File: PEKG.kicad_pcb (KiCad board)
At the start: 2 copper layers, 90 x 45 mm, 116 parts, among them J1 AudioJack4, J2 AudioJack3_SwitchTR, U1 TLV9062, U12 NCS21802DMR2G, U13 NCS21802DMR2G, U2 TLV9062, U3 INA350CDSIDDFR, U7 TLV61070ADBVR, U8 NCS21802DMR2G

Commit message: added sw
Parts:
- removed C21: 10n, Capacitor_SMD:C_0603_1608Metric_Pad1.08x0.95mm_HandSolder
- removed C22, C41: 10u, Capacitor_SMD:C_0603_1608Metric_Pad1.08x0.95mm_HandSolder
- removed C46: 100n, Capacitor_SMD:C_0603_1608Metric_Pad1.08x0.95mm_HandSolder
- removed JP1, JP7: Jumper_2_Bridged, Jumper:SolderJumper-2_P1.3mm_Bridged_RoundedPad1.0x1.5mm
- removed JP10, JP2, JP8: Jumper_2_Open, Jumper:SolderJumper-2_P1.3mm_Open_RoundedPad1.0x1.5mm
- removed L3: 4.7u, Inductor_SMD:L_Bourns_SRN6045TA
- removed R23, R32, R57: 100k, Resistor_SMD:R_0603_1608Metric_Pad0.98x0.95mm_HandSolder
- removed R35, R62, R63: 10k, Resistor_SMD:R_0603_1608Metric_Pad0.98x0.95mm_HandSolder
- removed R61: 1Meg, Resistor_SMD:R_0603_1608Metric_Pad0.98x0.95mm_HandSolder
- removed TP11: TestPoint, TestPoint:TestPoint_Pad_D3.0mm
- removed U13: NCS21802DMR2G, Package_SO:OnSemi_Micro8
- removed U3: INA350CDSIDDFR, Package_SO:MSOP-8_3x3mm_P0.65mm
- removed U7: TLV61070ADBVR, Package_TO_SOT_SMD:SOT-23-6_Handsoldering
- added SW1: SW_DPDT_x2, PEKG:DPDT_bigger, F.Cu at (159.0, 150.9)
- added U4: TLV9062, Package_SO:SOIC-8_3.9x4.9mm_P1.27mm, F.Cu at (152.3, 86.6)
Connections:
- net GAIN_5000_OUTPUT renamed GAIN_50
- C16 pad 2: Net-(U1A--) -> Net-(U12B--)
- C28 pad 2: Net-(JP2-A) -> DC_COMPENSATION
- JP3 pad 1: GAIN_500_OUTPUT -> GAIN_5
- JP9 pad 2: GAIN_500_OUTPUT -> GAIN_5
- R26 pad 2: Net-(U1A--) -> Net-(U12B--)
- R51 pad 1: Net-(U1A--) -> Net-(U12B--)
- R55 pad 2: Net-(JP2-A) -> DC_COMPENSATION
- R60 pad 1: Net-(U1A--) -> Net-(U12B--)
- U1 pad 1: Net-(JP4-A) -> (no net)
- U1 pad 2: Net-(U1A--) -> (no net)
- U1 pad 3: GAIN_500_OUTPUT -> (no net)
- U1 pad 5: GAIN_50_OUTPUT -> (no net)
- U1 pad 6: Net-(U1B--) -> (no net)
- U1 pad 7: Net-(JP10-A) -> (no net)
- U12 pad 5: V_{ref} -> GAIN_5
- U12 pad 6: COMMON_INPUT_LEVEL -> Net-(U12B--)
- U12 pad 7: Net-(C25-Pad2) -> Net-(JP4-A)
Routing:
- net (no net): track 0.00 -> 52.4 mm, vias 0 -> 2
- net GAIN_50_OUTPUT: track 29.6 -> 0.00 mm, vias 2 -> 0
- net GAIN_500_OUTPUT: track 13.5 -> 0.00 mm
- net GAIN_5: track 0.00 -> 13.5 mm
- net Net-(JP2-A): track 10.2 -> 0.00 mm
- net DC_COMPENSATION: track 42.4 -> 52.6 mm
- net Net-(JP10-A): track 9.98 -> 0.00 mm
- net Net-(U1B--): track 6.79 -> 0.00 mm
- net Net-(U1A--): track 6.75 -> 0.00 mm
- net Net-(U12B--): track 0.00 -> 6.75 mm
- net /FB: track 3.86 -> 0.00 mm
- net /SW_OUT: track 2.11 -> 0.00 mm
- added copper zone on F.Cu, net (none)
- removed copper zone on F.Cu, net /SW
- removed copper zone on F.Cu, net /SW_OUT

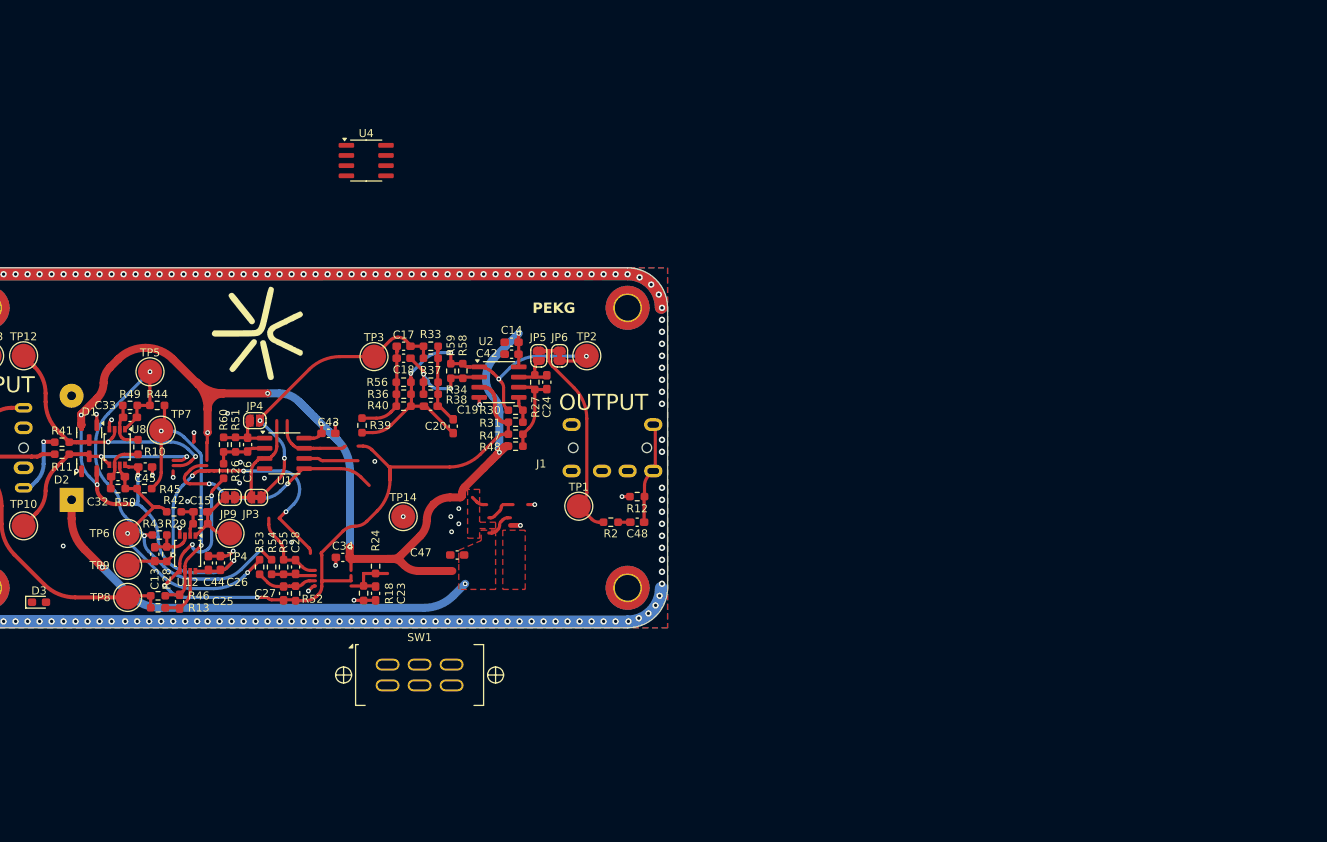
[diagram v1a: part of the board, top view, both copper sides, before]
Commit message: added notes, changed opamps
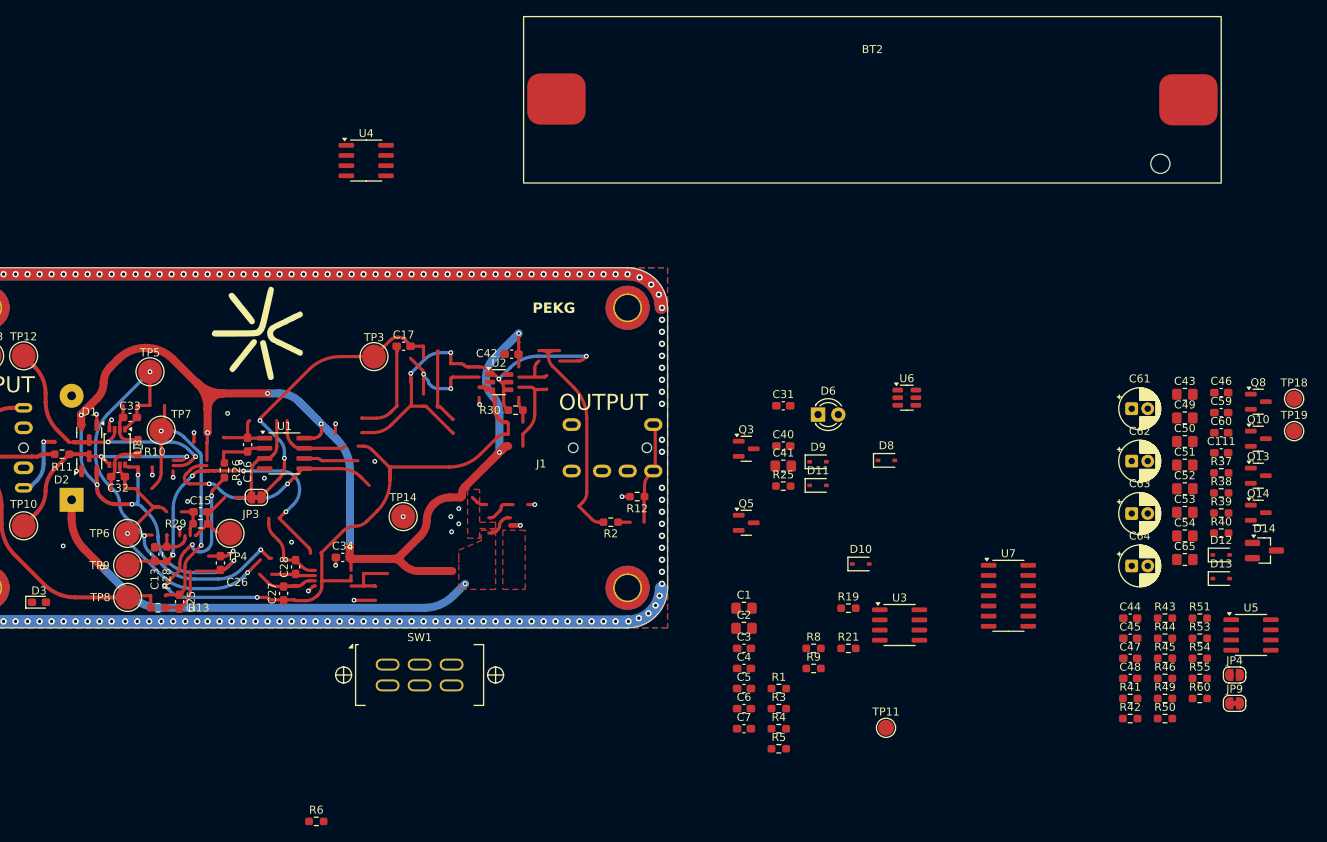
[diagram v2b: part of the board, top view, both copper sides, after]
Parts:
- removed C14, C23: 10u, Capacitor_SMD:C_0603_1608Metric_Pad1.08x0.95mm_HandSolder
- removed C18, C19, C20, C24: 10n, Capacitor_SMD:C_0603_1608Metric_Pad1.08x0.95mm_HandSolder
- removed JP5: Jumper_2_Open, Jumper:SolderJumper-2_P1.3mm_Open_RoundedPad1.0x1.5mm
- removed JP6: Jumper_2_Bridged, Jumper:SolderJumper-2_P1.3mm_Bridged_RoundedPad1.0x1.5mm
- removed R18, R24, R52: 100k, Resistor_SMD:R_0603_1608Metric_Pad0.98x0.95mm_HandSolder
- removed R27, R31: 10k, Resistor_SMD:R_0603_1608Metric_Pad0.98x0.95mm_HandSolder
- removed R33, R34, R56, R59: 10Meg, Resistor_SMD:R_0603_1608Metric_Pad0.98x0.95mm_HandSolder
- removed R36, R58: 330k, Resistor_SMD:R_0603_1608Metric_Pad0.98x0.95mm_HandSolder
- removed R47, R48: 20k, Resistor_SMD:R_0603_1608Metric_Pad0.98x0.95mm_HandSolder
- removed TP1, TP2: TestPoint, TestPoint:TestPoint_Pad_D3.0mm
- removed U12: NCS21802DMR2G, Package_SO:OnSemi_Micro8
- added BT2: Battery_Cell, PEKG:battery_holder, F.Cu at (215.6, 79.0)
- added C1: 10u, Resistor_SMD:R_0805_2012Metric_Pad1.20x1.40mm_HandSolder, F.Cu at (199.6, 142.6)
- added C111: 100n, Capacitor_SMD:C_0603_1608Metric_Pad1.08x0.95mm_HandSolder, F.Cu at (259.2, 123.1)
- added C2: 10u, Resistor_SMD:R_0805_2012Metric_Pad1.20x1.40mm_HandSolder, F.Cu at (199.6, 145.1)
- added C3: 100n, Capacitor_SMD:C_0603_1608Metric_Pad1.08x0.95mm_HandSolder, F.Cu at (199.6, 147.6)
- added C31: 100n, Capacitor_SMD:C_0603_1608Metric_Pad1.08x0.95mm_HandSolder, F.Cu at (204.5, 117.2)
- added C4: 100n, Capacitor_SMD:C_0603_1608Metric_Pad1.08x0.95mm_HandSolder, F.Cu at (199.6, 150.1)
- added C40: 1u, Capacitor_SMD:C_0603_1608Metric_Pad1.08x0.95mm_HandSolder, F.Cu at (204.5, 122.3)
- added C41: 10u, Resistor_SMD:R_0805_2012Metric_Pad1.20x1.40mm_HandSolder, F.Cu at (204.5, 124.8)
- added C46: 1u, Capacitor_SMD:C_0603_1608Metric_Pad1.08x0.95mm_HandSolder, F.Cu at (259.2, 115.6)
- added C49: 10u, Resistor_SMD:R_0805_2012Metric_Pad1.20x1.40mm_HandSolder, F.Cu at (254.7, 118.8)
- added C5: 100p, Capacitor_SMD:C_0603_1608Metric_Pad1.08x0.95mm_HandSolder, F.Cu at (199.6, 152.6)
- added C50: 10u, Resistor_SMD:R_0805_2012Metric_Pad1.20x1.40mm_HandSolder, F.Cu at (254.7, 121.7)
- added C51: 10u, Resistor_SMD:R_0805_2012Metric_Pad1.20x1.40mm_HandSolder, F.Cu at (254.7, 124.7)
- added C52: 10u, Resistor_SMD:R_0805_2012Metric_Pad1.20x1.40mm_HandSolder, F.Cu at (254.7, 127.6)
- added C53: 10u, Resistor_SMD:R_0805_2012Metric_Pad1.20x1.40mm_HandSolder, F.Cu at (254.7, 130.6)
- added C54: 10u, Resistor_SMD:R_0805_2012Metric_Pad1.20x1.40mm_HandSolder, F.Cu at (254.7, 133.5)
- added C59: 100n, Capacitor_SMD:C_0603_1608Metric_Pad1.08x0.95mm_HandSolder, F.Cu at (259.2, 118.1)
- added C6: 100n, Capacitor_SMD:C_0603_1608Metric_Pad1.08x0.95mm_HandSolder, F.Cu at (199.6, 155.1)
- added C60: 100n, Capacitor_SMD:C_0603_1608Metric_Pad1.08x0.95mm_HandSolder, F.Cu at (259.2, 120.6)
- added C61: 47u, Capacitor_THT:CP_Radial_D5.0mm_P2.00mm, F.Cu at (248.0, 117.6)
- added C62: 47u, Capacitor_THT:CP_Radial_D5.0mm_P2.00mm, F.Cu at (248.0, 124.2)
- added C63: 47u, Capacitor_THT:CP_Radial_D5.0mm_P2.00mm, F.Cu at (248.0, 130.7)
- added C64: 47u, Capacitor_THT:CP_Radial_D5.0mm_P2.00mm, F.Cu at (248.0, 137.3)
- added C65: 10u, Resistor_SMD:R_0805_2012Metric_Pad1.20x1.40mm_HandSolder, F.Cu at (254.7, 136.5)
- added C7: 100p, Capacitor_SMD:C_0603_1608Metric_Pad1.08x0.95mm_HandSolder, F.Cu at (199.6, 157.6)
- added D10: 1N4148WS, Diode_SMD:D_SOD-323, F.Cu at (214.2, 137.0)
- added D11: 1N4148WS, Diode_SMD:D_SOD-323, F.Cu at (208.8, 127.2)
- added D12: 1N4148WS, Diode_SMD:D_SOD-323, F.Cu at (259.2, 135.9)
- added D13: 1N4148WS, Diode_SMD:D_SOD-323, F.Cu at (259.2, 138.8)
- added D14: PSM712-LF-T7, Package_TO_SOT_SMD:SOT-23_Handsoldering, F.Cu at (264.6, 135.3)
- added D6: LED, LED_THT:LED_D3.0mm_FlatTop, F.Cu at (208.8, 118.3)
- added D8: 1N4148WS, Diode_SMD:D_SOD-323, F.Cu at (217.3, 124.1)
- added D9: 1N4148WS, Diode_SMD:D_SOD-323, F.Cu at (208.8, 124.2)
- added Q10: AO3401A, Package_TO_SOT_SMD:SOT-23, F.Cu at (263.8, 121.4)
- added Q13: AO3400A, Package_TO_SOT_SMD:SOT-23, F.Cu at (263.8, 126.0)
- added Q14: AO3400A, Package_TO_SOT_SMD:SOT-23, F.Cu at (263.8, 130.6)
- added Q3: AO3400A, Package_TO_SOT_SMD:SOT-23, F.Cu at (199.8, 122.6)
- added Q5: AO3400A, Package_TO_SOT_SMD:SOT-23, F.Cu at (199.8, 131.9)
- added Q8: AO3401A, Package_TO_SOT_SMD:SOT-23, F.Cu at (263.8, 116.7)
- added R1: 10k, Resistor_SMD:R_0603_1608Metric_Pad0.98x0.95mm_HandSolder, F.Cu at (203.9, 152.6)
- added R19: 39k, Resistor_SMD:R_0603_1608Metric_Pad0.98x0.95mm_HandSolder, F.Cu at (212.6, 142.6)
- added R21: 470k, Resistor_SMD:R_0603_1608Metric_Pad0.98x0.95mm_HandSolder, F.Cu at (212.6, 147.6)
- added R25: 10k, Resistor_SMD:R_0603_1608Metric_Pad0.98x0.95mm_HandSolder, F.Cu at (204.5, 127.3)
- added R3: 200k, Resistor_SMD:R_0603_1608Metric_Pad0.98x0.95mm_HandSolder, F.Cu at (203.9, 155.1)
- added R4: 200k, Resistor_SMD:R_0603_1608Metric_Pad0.98x0.95mm_HandSolder, F.Cu at (203.9, 157.6)
- added R5: 1k, Resistor_SMD:R_0603_1608Metric_Pad0.98x0.95mm_HandSolder, F.Cu at (203.9, 160.1)
- added R6: 1k, Resistor_SMD:R_0603_1608Metric_Pad0.98x0.95mm_HandSolder, F.Cu at (146.1, 169.2)
- added R8: 2.7k, Resistor_SMD:R_0603_1608Metric_Pad0.98x0.95mm_HandSolder, F.Cu at (208.2, 147.6)
- added R9: 1k, Resistor_SMD:R_0603_1608Metric_Pad0.98x0.95mm_HandSolder, F.Cu at (208.2, 150.1)
- added TP11: TestPoint, TestPoint:TestPoint_Pad_D2.0mm, F.Cu at (217.3, 157.5)
- added TP18: TestPoint, TestPoint:TestPoint_Pad_D2.0mm, F.Cu at (268.3, 116.4)
- added TP19: TestPoint, TestPoint:TestPoint_Pad_D2.0mm, F.Cu at (268.3, 120.4)
- added U3: OP07, Package_SO:SOIC-8_3.9x4.9mm_P1.27mm, F.Cu at (219.0, 144.7)
- added U5: NE5532, Package_SO:SOIC-8_3.9x4.9mm_P1.27mm, F.Cu at (262.9, 145.9)
- added U6: BQ21040DBV, Package_TO_SOT_SMD:SOT-23-6, F.Cu at (219.9, 116.2)
- added U7: 74HC14, Package_SO:SOIC-14_3.9x8.7mm_P1.27mm, F.Cu at (232.6, 141.0)
- C17: value 10n -> 1n
- C43: value 100n -> 10u; footprint Capacitor_SMD:C_0603_1608Metric_Pad1.08x0.95mm_HandSolder -> Resistor_SMD:R_0805_2012Metric_Pad1.20x1.40mm_HandSolder
- R30: value 10k -> 330
- R37, R38: value 330k -> 100k
- R39: value 10Meg -> 470k
- R40: value 330k -> 10k
- U1: value TLV9062 -> OP07
- U2: value TLV9062 -> AP9101CK6; footprint Package_SO:SOIC-8_3.9x4.9mm_P1.27mm -> Package_TO_SOT_SMD:SOT-23-6
- U4: value TLV9062 -> NE5532
- moved R41 137.3 mm to (247.8, 153.8)
- moved R49 134.5 mm to (252.2, 153.8)
- moved R50 134.0 mm to (252.2, 156.3), turned to 0 degrees
- moved R45 129.3 mm to (252.2, 148.8)
- moved R44 129.3 mm to (252.2, 146.3), turned to 0 degrees
- moved JP9 128.2 mm to (260.9, 154.4)
- moved JP4 126.5 mm to (260.9, 150.9)
- moved R46 126.3 mm to (252.2, 151.3)
- moved R43 126.1 mm to (252.2, 143.8)
- moved R60 126.1 mm to (256.5, 153.8), turned to 0 degrees
- moved C45 125.0 mm to (247.8, 146.3), turned to 0 degrees
- moved R51 122.5 mm to (256.5, 143.8), turned to 0 degrees
- moved R42 122.3 mm to (247.8, 156.3)
- moved R53 117.9 mm to (256.5, 146.3), turned to 0 degrees
- moved R54 116.6 mm to (256.5, 148.8), turned to 0 degrees
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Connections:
- C16 pad 2: Net-(U12B--) -> Net-(U4A--)
- C17 pad 1: Net-(C17-Pad1) -> Earth
- C17 pad 2: GAIN_50 -> Net-(D10-A)
- C27 pad 1: V_{ref} -> GND
- C32 pad 2: Net-(U8B--) -> Net-(U3--)
- C33 pad 1: Net-(U8A--) -> Net-(U1--)
- C42 pad 1: V_{cc} -> NMOS_GATE
- C42 pad 2: GND -> Net-(D13-A)
- C43 pad 1: GND -> /Power supply/MID_DRV
- C43 pad 2: V_{cc} -> /Power supply/MID_REC
- D3 pad 1: unconnected-(D3-K-Pad1) -> GND
- D3 pad 2: unconnected-(D3-A-Pad2) -> Net-(D3-A)
- R10 pad 1: Net-(U8B--) -> Net-(U3--)
- R10 pad 2: Net-(U8A--) -> Net-(U1--)
- R2 pad 2: LEVELED_OUTPUT -> FIL_OUT
- R26 pad 2: Net-(U12B--) -> Net-(U4A--)
- R30 pad 1: FIL_OUT -> +BATT
- R37 pad 1: Net-(C19-Pad2) -> Net-(D10-A)
- R37 pad 2: GAIN_50 -> Net-(D9-K)
- R38 pad 1: Net-(U2A--) -> Net-(D10-K)
- R38 pad 2: Net-(C19-Pad2) -> CLK
- R39 pad 1: FIL_OUT -> Net-(D10-K)
- R39 pad 2: Net-(C17-Pad1) -> CLK
- R40 pad 1: FIL_OUT -> Net-(D11-K)
- R40 pad 2: Net-(C17-Pad1) -> CLK
- R49 pad 1: Net-(U8A--) -> Net-(U1--)
- R50 pad 2: Net-(U8B--) -> Net-(U3--)
- R51 pad 1: Net-(U12B--) -> Net-(U4A--)
- R60 pad 1: Net-(U12B--) -> Net-(U4A--)
- SW1 pad 5: unconnected-(SW1B-B-Pad5) -> V_{cc}
- SW1 pad 6: unconnected-(SW1B-C-Pad6) -> Net-(SW1B-C)
- U1 pad 1: (no net) -> unconnected-(U1-VOS-Pad1)
- U1 pad 2: (no net) -> Net-(U1--)
- U1 pad 3: (no net) -> /LA_IN
- U1 pad 5: (no net) -> unconnected-(U1-NC-Pad5)
- U1 pad 6: (no net) -> /TOP
- U1 pad 7: (no net) -> V_{cc}
- U1 pad 8: V_{cc} -> unconnected-(U1-VOS-Pad8)
- U2 pad 1: FIL_OUT -> Net-(Q3-G)
- U2 pad 2: Net-(U2A--) -> Net-(U2-VM)
- U2 pad 3: V_{ref} -> Net-(Q5-G)
- U2 pad 4: GND -> unconnected-(U2-NC-Pad4)
- U2 pad 6: Net-(U2B--) -> -BATT
- U4 pad 1: V_{ref} -> Net-(JP4-A)
- U4 pad 2: V_{ref} -> Net-(U4A--)
- U4 pad 3: Net-(U4A-+) -> GAIN_5
- U8 pad 1: /TOP -> (no net)
- U8 pad 2: Net-(U8A--) -> (no net)
- U8 pad 3: /LA_IN -> (no net)
- U8 pad 5: /RA_IN -> (no net)
- U8 pad 6: Net-(U8B--) -> (no net)
- U8 pad 7: /BOTTOM -> (no net)
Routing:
- net unconnected-(U1-NC-Pad5): track 0.00 -> 29.6 mm, vias 0 -> 2
- net FIL_OUT: track 51.8 -> 81.0 mm
- net LEVELED_OUTPUT: track 29.2 -> 0.00 mm
- net Earth: track 0.00 -> 19.3 mm
- net Net-(U2A--): track 14.4 -> 0.00 mm, vias 2 -> 0
- net Net-(C17-Pad1): track 11.8 -> 0.00 mm
- net Net-(U2B--): track 11.4 -> 0.00 mm
- net V_{cc}: track 179.8 -> 189.8 mm
- net Net-(C19-Pad2): track 9.57 -> 0.00 mm
- net Net-(U4A-+): track 7.67 -> 0.00 mm
- net Net-(JP4-A): track 7.47 -> 0.00 mm
- net Net-(U8B--): track 6.83 -> 0.00 mm
- net Net-(U3--): track 0.00 -> 6.83 mm
- net /TOP: track 55.8 -> 62.6 mm
- net Net-(U4A--): track 0.00 -> 6.75 mm
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
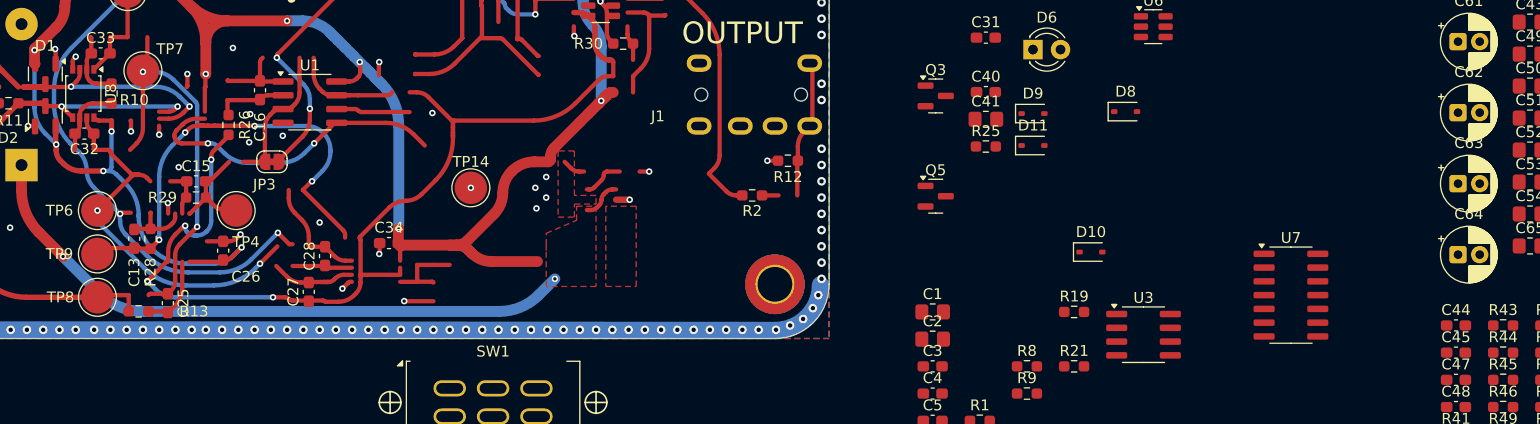
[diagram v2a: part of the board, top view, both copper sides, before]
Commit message: more readable schematic, bipolar supply
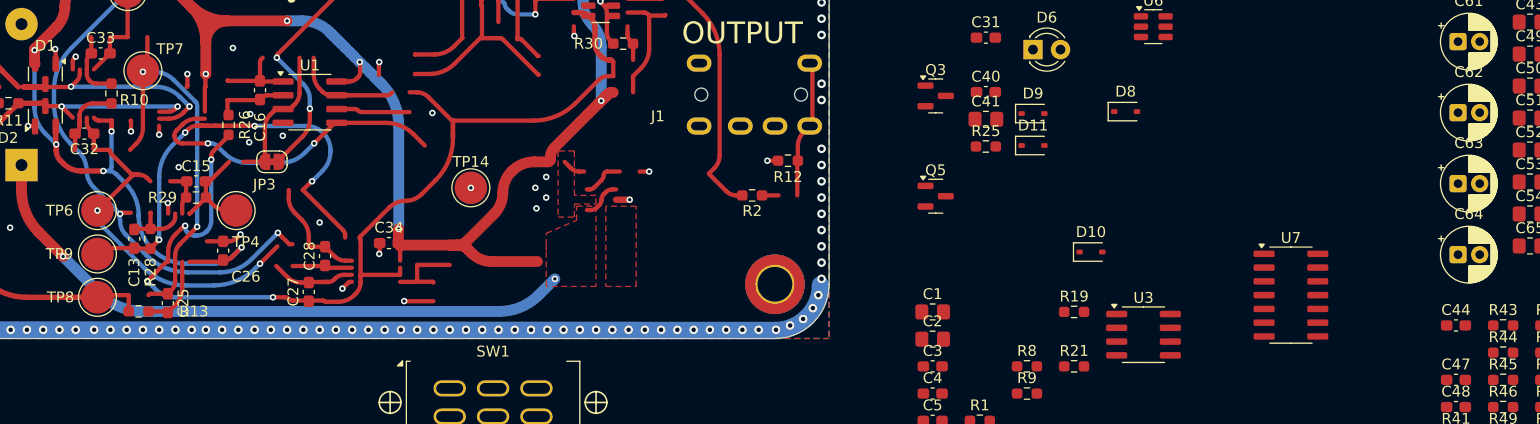
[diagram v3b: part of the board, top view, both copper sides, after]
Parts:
- removed C45: 100n, Capacitor_SMD:C_0603_1608Metric_Pad1.08x0.95mm_HandSolder
- removed U8: NCS21802DMR2G, Package_SO:OnSemi_Micro8
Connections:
- C1 pad 1: Earth -> 0
- C1 pad 2: -VIN -> V_{ee}
- C111 pad 1: Earth -> 0
- C111 pad 2: +VIN -> V_{cc}
- C17 pad 1: Earth -> 0
- C26 pad 2: GND -> V_{ee}
- C3 pad 1: Earth -> 0
- C31 pad 1: Earth -> 0
- C31 pad 2: +VIN -> V_{cc}
- C34 pad 1: GND -> V_{ee}
- C40 pad 1: Earth -> 0
- C44 pad 1: GND -> V_{ee}
- C46 pad 1: Earth -> 0
- C46 pad 2: +VIN -> V_{cc}
- C5 pad 1: Earth -> 0
- C51 pad 1: Earth -> 0
- C51 pad 2: -VIN -> V_{ee}
- C52 pad 1: Earth -> 0
- C52 pad 2: -VIN -> V_{ee}
- C53 pad 1: Earth -> 0
- C53 pad 2: -VIN -> V_{ee}
- C54 pad 1: Earth -> 0
- C54 pad 2: -VIN -> V_{ee}
- C59 pad 1: Earth -> 0
- C59 pad 2: -VIN -> V_{ee}
- C63 pad 1: Earth -> 0
- C63 pad 2: -VIN -> V_{ee}
- C64 pad 1: Earth -> 0
- C64 pad 2: -VIN -> V_{ee}
- C7 pad 1: Earth -> 0
- D13 pad 1: Earth -> 0
- D8 pad 1: Earth -> 0
- Q10 pad 2: Earth -> 0
- Q13 pad 2: Earth -> 0
- Q14 pad 2: -VIN -> V_{ee}
- Q5 pad 2: Earth -> 0
- Q8 pad 2: +VIN -> V_{cc}
- R25 pad 2: Earth -> 0
- R6 pad 1: Earth -> 0
- R8 pad 1: Earth -> 0
- U1 pad 4: GND -> V_{ee}
- U3 pad 4: GND -> V_{ee}
- U4 pad 4: GND -> V_{ee}
- U5 pad 4: GND -> V_{ee}
- U6 pad 5: Earth -> 0
- U7 pad 14: +VIN -> V_{cc}
- U7 pad 7: Earth -> 0
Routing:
- net Earth: track 19.3 -> 7.47 mm
- net 0: track 0.00 -> 11.8 mm
- net GND: track 20.8 -> 16.4 mm, vias 193 -> 191
- net V_{ee}: track 0.00 -> 4.32 mm, vias 0 -> 2

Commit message: Added ESP32-S3
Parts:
- removed BT1: Battery_Cell, PEKG:MG_battery_holder
- removed D14: PSM712-LF-T7, Package_TO_SOT_SMD:SOT-23_Handsoldering
- added D4: 1N5819WS, Diode_SMD:D_SOD-323, F.Cu at (62.8, 127.5)
- added JP10: Jumper_2_Bridged, Jumper:SolderJumper-2_P1.3mm_Bridged_RoundedPad1.0x1.5mm, F.Cu at (62.8, 124.3)
- added U11: AP9101CK6, Package_TO_SOT_SMD:SOT-23-6_Handsoldering, F.Cu at (63.5, 118.2)
- added U8: 74HC14, Package_SO:SOIC-14_3.9x8.7mm_P1.27mm, F.Cu at (413.6, 102.2)
- BT2: moved to B.Cu
- U2: value AP9101CK6 -> ESP32-S3-ZERO; footprint Package_TO_SOT_SMD:SOT-23-6 -> PEKG:MODULE_ESP32-S3-ZERO; moved to B.Cu
- moved C1 218.6 mm to (418.1, 138.4)
- moved C16 218.6 mm to (356.1, 118.0)
- moved C17 218.6 mm to (375.6, 105.7)
- moved C2 218.6 mm to (418.1, 141.0)
- moved C25 218.6 mm to (347.6, 137.6)
- moved C27 218.6 mm to (360.6, 136.6)
- moved C28 218.6 mm to (362.1, 133.3)
- moved C3 218.6 mm to (418.1, 143.5)
- moved C32 218.6 mm to (339.9, 122.0)
- moved C33 218.6 mm to (341.4, 114.6)
- moved C4 218.6 mm to (418.1, 146.0)
- moved C42 218.6 mm to (389.1, 106.7)
- moved C5 218.6 mm to (418.1, 148.5)
- moved C6 218.6 mm to (418.1, 151.0)
- moved D1 218.6 mm to (336.2, 116.5)
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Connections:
- net +VBUS renamed +V_{USB}
- BT2 pad 1: +BATT -> +V_{BAT}
- C6 pad 2: Net-(U2-VDD) -> Net-(U11-VDD)
- R30 pad 1: +BATT -> +V_{BAT}
- R30 pad 2: Net-(U2-VDD) -> Net-(U11-VDD)
- R8 pad 2: Net-(U2-VM) -> Net-(U11-VM)
- U2 pad 1: Net-(Q3-G) -> unconnected-(U2-GP1-Pad1)
- U2 pad 2: Net-(U2-VM) -> unconnected-(U2-GP2-Pad2)
- U2 pad 3: Net-(Q5-G) -> unconnected-(U2-GP3-Pad3)
- U2 pad 5: Net-(U2-VDD) -> unconnected-(U2-GP5-Pad5)
- U2 pad 6: -BATT -> unconnected-(U2-GP6-Pad6)
- U6 pad 2: +BATT -> +V_{BAT}
- U7 pad 1: Net-(D12-A) -> unconnected-(U7-Pad1)
- U7 pad 10: NMOS_GATE -> (no net)
- U7 pad 11: Net-(D11-K) -> (no net)
- U7 pad 12: NMOS_GATE -> (no net)
- U7 pad 13: Net-(D11-K) -> (no net)
- U7 pad 14: V_{cc} -> (no net)
- U7 pad 2: PMOS_GATE -> unconnected-(U7-Pad2)
- U7 pad 3: Net-(D12-A) -> (no net)
- U7 pad 4: PMOS_GATE -> (no net)
- U7 pad 5: Net-(D12-A) -> (no net)
- U7 pad 6: PMOS_GATE -> (no net)
- U7 pad 7: 0 -> (no net)
- U7 pad 8: CLK -> (no net)
- U7 pad 9: Net-(D10-A) -> (no net)
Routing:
- net V_{cc}: track 189.8 -> 0.00 mm, vias 11 -> 0
- net V_{ref}: track 94.1 -> 0.00 mm, vias 4 -> 0
- net FIL_OUT: track 81.0 -> 0.00 mm, vias 4 -> 0
- net /TOP: track 62.6 -> 0.00 mm, vias 3 -> 0
- net VBAT: track 61.6 -> 0.00 mm, vias 2 -> 0
- net (no net): track 54.5 -> 0.00 mm, vias 2 -> 0
- net DC_COMPENSATION: track 52.6 -> 0.00 mm, vias 4 -> 0
- net RIGHT_LEG_DRIVE: track 44.8 -> 0.00 mm
- net GAIN_50: track 38.3 -> 0.00 mm, vias 2 -> 0
- net COMMON_INPUT_LEVEL: track 37.4 -> 0.00 mm, vias 2 -> 0
- net /LA_IN: track 35.8 -> 0.00 mm, vias 2 -> 0
- net /BOTTOM: track 35.7 -> 0.00 mm, vias 2 -> 0
- net unconnected-(U1-NC-Pad5): track 29.6 -> 0.00 mm, vias 2 -> 0
- net /RA_IN: track 29.0 -> 0.00 mm, vias 2 -> 0
- net GND: track 16.4 -> 0.00 mm, vias 191 -> 0
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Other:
- board size 90 x 45 mm -> 90 x 60 mm
